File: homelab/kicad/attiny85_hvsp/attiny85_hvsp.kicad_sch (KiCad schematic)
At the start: 3 parts, among them U1 MC33063AD

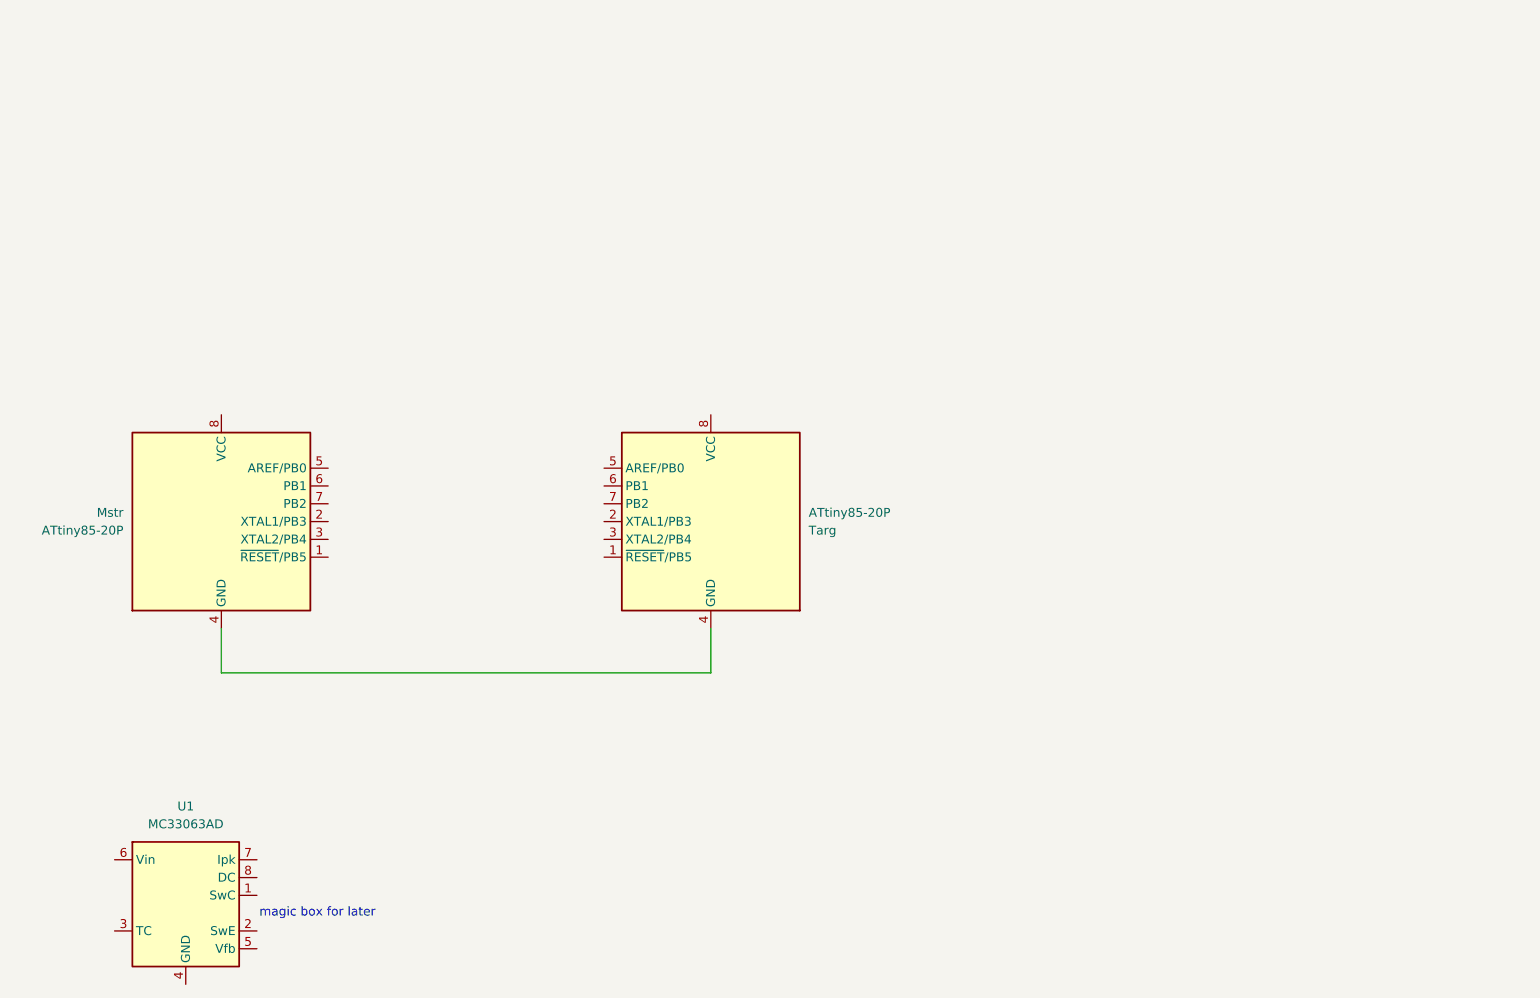
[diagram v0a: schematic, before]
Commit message: finalized ic selection
incomplete boost converter circuit
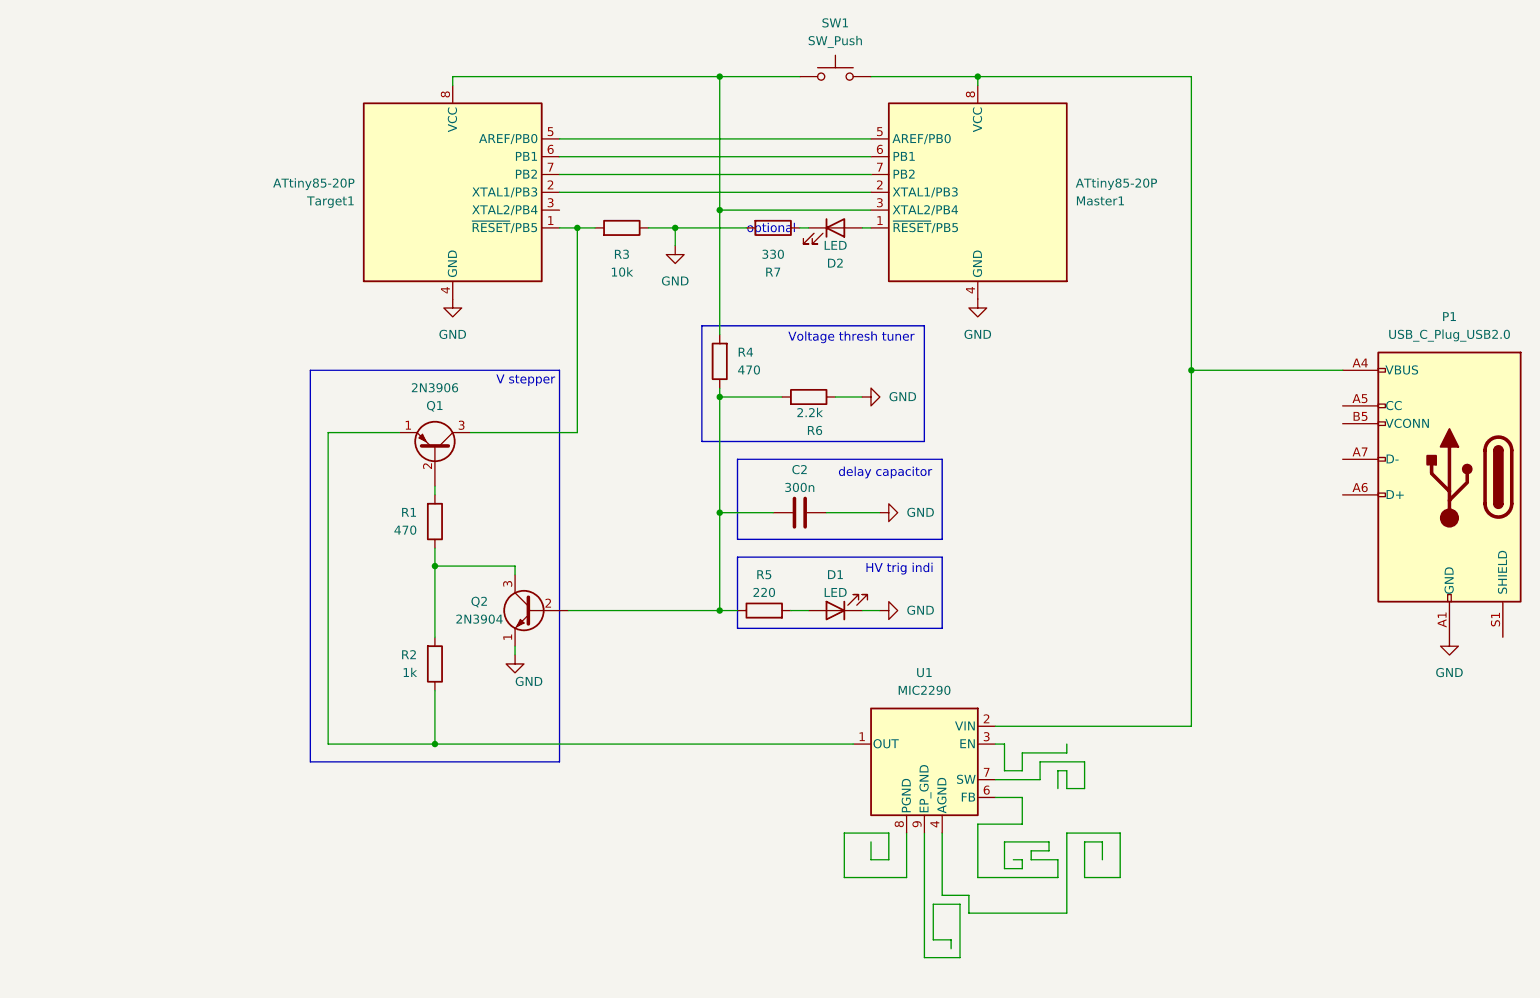
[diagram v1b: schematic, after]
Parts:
- removed Mstr: ATtiny85-20P, Package_DIP:DIP-8_W7.62mm, symbol MCU_Microchip_ATtiny:ATtiny85-20P
- removed U1: MC33063AD, Package_SO:SOIC-8_3.9x4.9mm_P1.27mm, symbol Regulator_Switching:MC33063AD
- added C2: 300n, symbol Device:C
- added D1, D2: LED, LED_THT:LED_Rectangular_W3.0mm_H2.0mm, symbol Device:LED
- added P1: USB_C_Plug_USB2.0, symbol Connector:USB_C_Plug_USB2.0
- added Q1: 2N3906, Package_TO_SOT_THT:TO-92_Inline, symbol Transistor_BJT:2N3906
- added Q2: 2N3904, Package_TO_SOT_THT:TO-92_Inline, symbol Transistor_BJT:2N3904
- added R1, R4: 470, symbol Device:R
- added R2: 1k, symbol Device:R
- added R3: 10k, symbol Device:R
- added R5: 220, symbol Device:R
- added R6: 2.2k, symbol Device:R
- added R7: 330, symbol Device:R
- added SW1: SW_Push, Button_Switch_SMD:Nidec_Copal_CAS-120A, symbol Switch:SW_Push
- added Target1: ATtiny85-20P, Package_DIP:DIP-8_W7.62mm, symbol MCU_Microchip_ATtiny:ATtiny85-20P
- added U1: MIC2290, Package_DFN_QFN:Micrel_MLF-8-1EP_2x2mm_P0.5mm_EP0.8x1.3mm_ThermalVias, symbol Regulator_Switching:MIC2290
- renumbered Targ to Master1
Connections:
- net at Master1.1 (~{RESET}/PB5): now also D2.2 (A)
- net at Master1.2 (XTAL1/PB3): now also Target1.2 (XTAL1/PB3)
- net at Master1.3 (XTAL2/PB4): now also R4.2, SW1.1, Target1.8 (VCC)
- net GND: now reaches Master1.4 (GND)
- net GND: now also C2.2, D1.1 (K), P1.A1 (GND), P1.A12 (GND), P1.B1 (GND), P1.B12 (GND), Q2.1 (E), R3.1, R6.1, R7.2, Target1.4 (GND)
- net at Master1.5 (AREF/PB0): now also Target1.5 (AREF/PB0)
- net at Master1.6 (PB1): now also Target1.6 (PB1)
- net at Master1.7 (PB2): now also Target1.7 (PB2)
- net at Master1.8 (VCC): now also P1.A4 (VBUS), P1.A9 (VBUS), P1.B4 (VBUS), P1.B9 (VBUS), SW1.2, U1.2 (VIN)
- new net: Q2.3 (C), R1.1, R2.2
- new net: Q1.2 (B), R1.2
- new net: Q1.3 (C), R3.2, Target1.1 (~{RESET}/PB5)
- new net: C2.1, Q2.2 (B), R4.1, R5.1, R6.2
- new net: D1.2 (A), R5.2
- new net: Q1.1 (E), R2.1, U1.1 (OUT)
- new net: D2.1 (K), R7.1
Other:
- note added: "HV trig indi"
- note added: "V stepper"
- note added: "Voltage thresh tuner"
- note added: "delay capacitor"
- note added: "optional"
- note removed: "magic box for later"
- moved on the sheet: Master1

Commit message: finalized 2 stage bjt v stepper. fet would have been better but gotta use these bjts for something
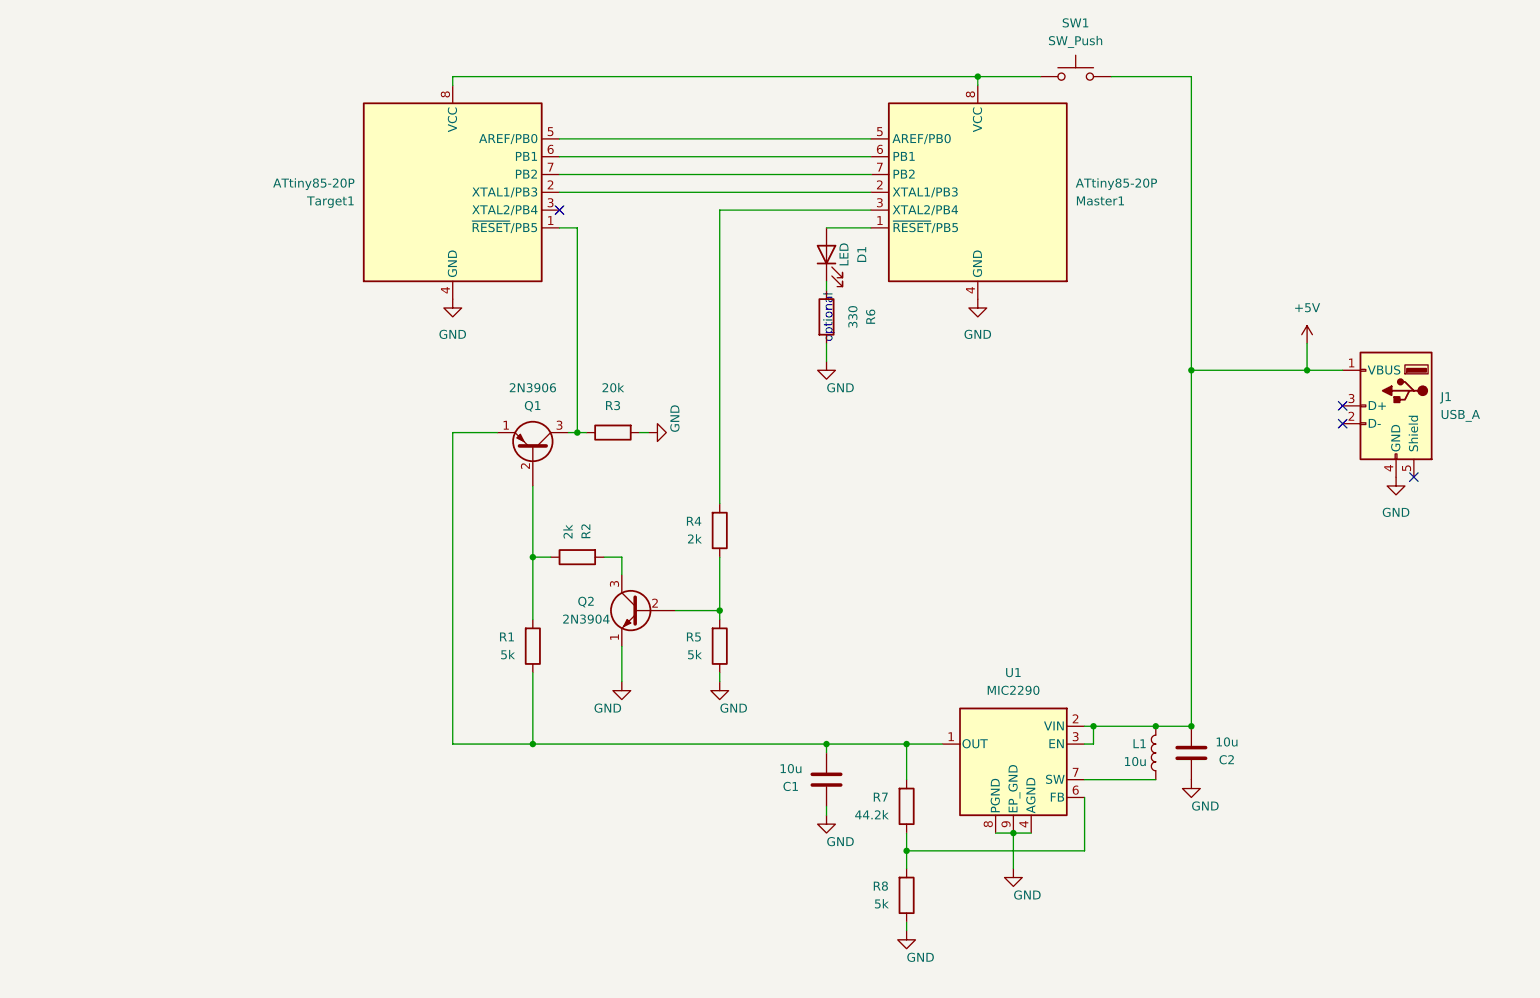
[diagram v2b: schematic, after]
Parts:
- removed D1: LED, LED_THT:LED_Rectangular_W3.0mm_H2.0mm, symbol Device:LED
- removed P1: USB_C_Plug_USB2.0, symbol Connector:USB_C_Plug_USB2.0
- removed R6: 2.2k, symbol Device:R
- added C1: 10u, Capacitor_SMD:C_1210_3225Metric, symbol Device:C
- added J1: USB_A, Connector_USB:USB_A_Molex_48037-2200_Horizontal, symbol Connector:USB_A
- added L1: 10u, miscellaneous:IDCP2218-01, symbol Device:L
- added R7: 44.2k, Resistor_SMD:R_1206_3216Metric, symbol Device:R
- added R8: 5k, Resistor_SMD:R_0805_2012Metric, symbol Device:R
- C2: value 300n -> 10u; footprint (none) -> Capacitor_SMD:C_1210_3225Metric
- R1: renamed from R2; value 1k -> 5k; footprint (none) -> Resistor_SMD:R_0805_2012Metric
- R2: renamed from R1; value 470 -> 2k; footprint (none) -> Resistor_SMD:R_0603_1608Metric
- R3: value 10k -> 20k; footprint (none) -> Resistor_SMD:R_0805_2012Metric
- R4: value 470 -> 2k; footprint (none) -> Resistor_SMD:R_0603_1608Metric
- R5: value 220 -> 5k; footprint (none) -> Resistor_SMD:R_0805_2012Metric
- R6: renamed from R7; footprint (none) -> Resistor_SMD:R_2010_5025Metric
- SW1: footprint Button_Switch_SMD:Nidec_Copal_CAS-120A -> Button_Switch_SMD:SW_SPST_Omron_B3FS-101xP
- renumbered D2 to D1
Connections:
- net GND: now also R3.2, R5.1, U1.4 (AGND), U1.8 (PGND), U1.9 (EP_GND), C1.2, J1.4 (GND), R8.1; no longer R3.1
- net at R1.2, R2.1: now also Q1.2 (B); no longer Q2.3 (C)
- net at R2.2: now also Q2.3 (C); no longer Q1.2 (B)
- net at Q1.3 (C), Target1.1 (~{RESET}/PB5): now also R3.1; no longer R3.2
- net at SW1.1, Target1.8 (VCC): now also Master1.8 (VCC); no longer Master1.3 (XTAL2/PB4), R4.2
- net at Q2.2 (B), R4.1: now also R5.2; no longer C2.1, R5.1
- net +5V: now reaches SW1.2, U1.2 (VIN)
- net +5V: now also C2.1, U1.3 (EN), J1.1 (VBUS), L1.1; no longer Master1.8 (VCC)
- net at Q1.1 (E), R1.1, U1.1 (OUT): now also C1.1, R7.2
- net at U1.6 (FB): now also R7.1, R8.2
- net at U1.7 (SW): now also L1.2
- new net: Master1.3 (XTAL2/PB4), R4.2
- no-connect marks 0 -> 4
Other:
- note removed: "HV trig indi"
- note removed: "V stepper"
- note removed: "Voltage thresh tuner"
- note removed: "delay capacitor"
- moved on the sheet: D1, Q1, Q2, R1, R2, R3, R6, SW1, U1

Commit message: forgot ot push schematic
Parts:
- U1: footprint Package_DFN_QFN:Micrel_MLF-8-1EP_2x2mm_P0.5mm_EP0.8x1.3mm_ThermalVias -> Package_DFN_QFN:Micrel_MLF-8-1EP_2x2mm_P0.5mm_EP0.6x1.2mm
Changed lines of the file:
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@@
 			)
 		)
-		(property "Footprint" "Package_DFN_QFN:Micrel_MLF-8-1EP_2x2mm_P0.5mm_EP0.8x1.3mm_ThermalVias"
+		(property "Footprint" "Package_DFN_QFN:Micrel_MLF-8-1EP_2x2mm_P0.5mm_EP0.6x1.2mm"
 			(at 218.44 149.86 0)
 			(effects

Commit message: maybe bantam safe layout
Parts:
- Q1, Q2: footprint Package_TO_SOT_THT:TO-92_Inline -> Package_TO_SOT_THT:TO-92L_HandSolder
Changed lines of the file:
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@@
 			)
 		)
-		(property "Footprint" "Package_TO_SOT_THT:TO-92_Inline"
+		(property "Footprint" "Package_TO_SOT_THT:TO-92L_HandSolder"
 			(at 116.205 81.28 0)
 			(effects
@@
 			)
 		)
-		(property "Footprint" "Package_TO_SOT_THT:TO-92_Inline"
+		(property "Footprint" "Package_TO_SOT_THT:TO-92L_HandSolder"
 			(at 128.27 111.125 0)
 			(effects

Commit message: athvsp
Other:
- note added: "maybe"
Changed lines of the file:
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@@
+		)
+	)
+	(text "maybe"
+		(exclude_from_sim no)
+		(at 129.794 84.074 0)
+		(effects
+			(font
+				(size 1.27 1.27)
+			)
 		)
 	)
